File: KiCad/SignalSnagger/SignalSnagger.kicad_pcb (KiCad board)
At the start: 2 copper layers, 133.4 x 44.3 mm, 4 parts

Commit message: Rev 0.28
Adding footprints to schematic: ~10% done
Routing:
- added copper zone on In1.Cu, net (none)
- added copper zone on In2.Cu, net (none)
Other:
- copper layers 2 -> 4
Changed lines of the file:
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@@
 (kicad_pcb (version 20211014) (generator pcbnew)
   (general
-    (thickness 1.6)
+    (thickness 4.69)
   )
   (paper "A4")
   (layers
     (0 "F.Cu" signal)
+    (1 "In1.Cu" signal)
+    (2 "In2.Cu" signal)
     (31 "B.Cu" signal)
     (32 "B.Adhes" user "B.Adhesive")
@@
   )
   (setup
+    (stackup
+      (layer "F.SilkS" (type "Top Silk Screen"))
+      (layer "F.Paste" (type "Top Solder Paste"))
+      (layer "F.Mask" (type "Top Solder Mask") (thickness 0.01))
+      (layer "F.Cu" (type "copper") (thickness 0.035))
+      (layer "dielectric 1" (type "core") (thickness 1.51) (material "FR4") (epsilon_r 4.5) (loss_tangent 0.02))
+      (layer "In1.Cu" (type "copper") (thickness 0.035))
+      (layer "dielectric 2" (type "prepreg") (thickness 1.51) (material "FR4") (epsilon_r 4.5) (loss_tangent 0.02))
+      (layer "In2.Cu" (type "copper") (thickness 0.035))
+      (layer "dielectric 3" (type "core") (thickness 1.51) (material "FR4") (epsilon_r 4.5) (loss_tangent 0.02))
+      (layer "B.Cu" (type "copper") (thickness 0.035))
+      (layer "B.Mask" (type "Bottom Solder Mask") (thickness 0.01))
+      (layer "B.Paste" (type "Bottom Solder Paste"))
+      (layer "B.SilkS" (type "Bottom Silk Screen"))
+      (copper_finish "None")
+      (dielectric_constraints no)
+    )
     (pad_to_mask_clearance 0)
     (pcbplotparams
@@
     )
   )
+  (zone locked (net 0) (net_name "") (layers "In1.Cu" "In2.Cu") (hatch edge 0.508)
+    (connect_pads (clearance 0.508))
+    (min_thickness 0.254) (filled_areas_thickness no)
+    (fill yes (thermal_gap 0.508) (thermal_bridge_width 0.508))
+    (polygon
+      (pts
+        (xy 210.24 115.69)
+        (xy 208.01 117.92)
+        (xy 80.01 117.98)
+        (xy 77.69 115.66)
+        (xy 77.68 76.65)
+        (xy 79.99 74.38)
+        (xy 208 74.37)
+        (xy 210.25 76.61)
+      )
+    )
+  )
   (zone locked (net 0) (net_name "") (layer "B.Cu") (hatch edge 0.508)
     (connect_pads (clearance 0.508))
     (min_thickness 0.254) (filled_areas_thickness no)
-    (fill (thermal_gap 0.508) (thermal_bridge_width 0.508))
+    (fill yes (thermal_gap 0.508) (thermal_bridge_width 0.508))
     (polygon
       (pts

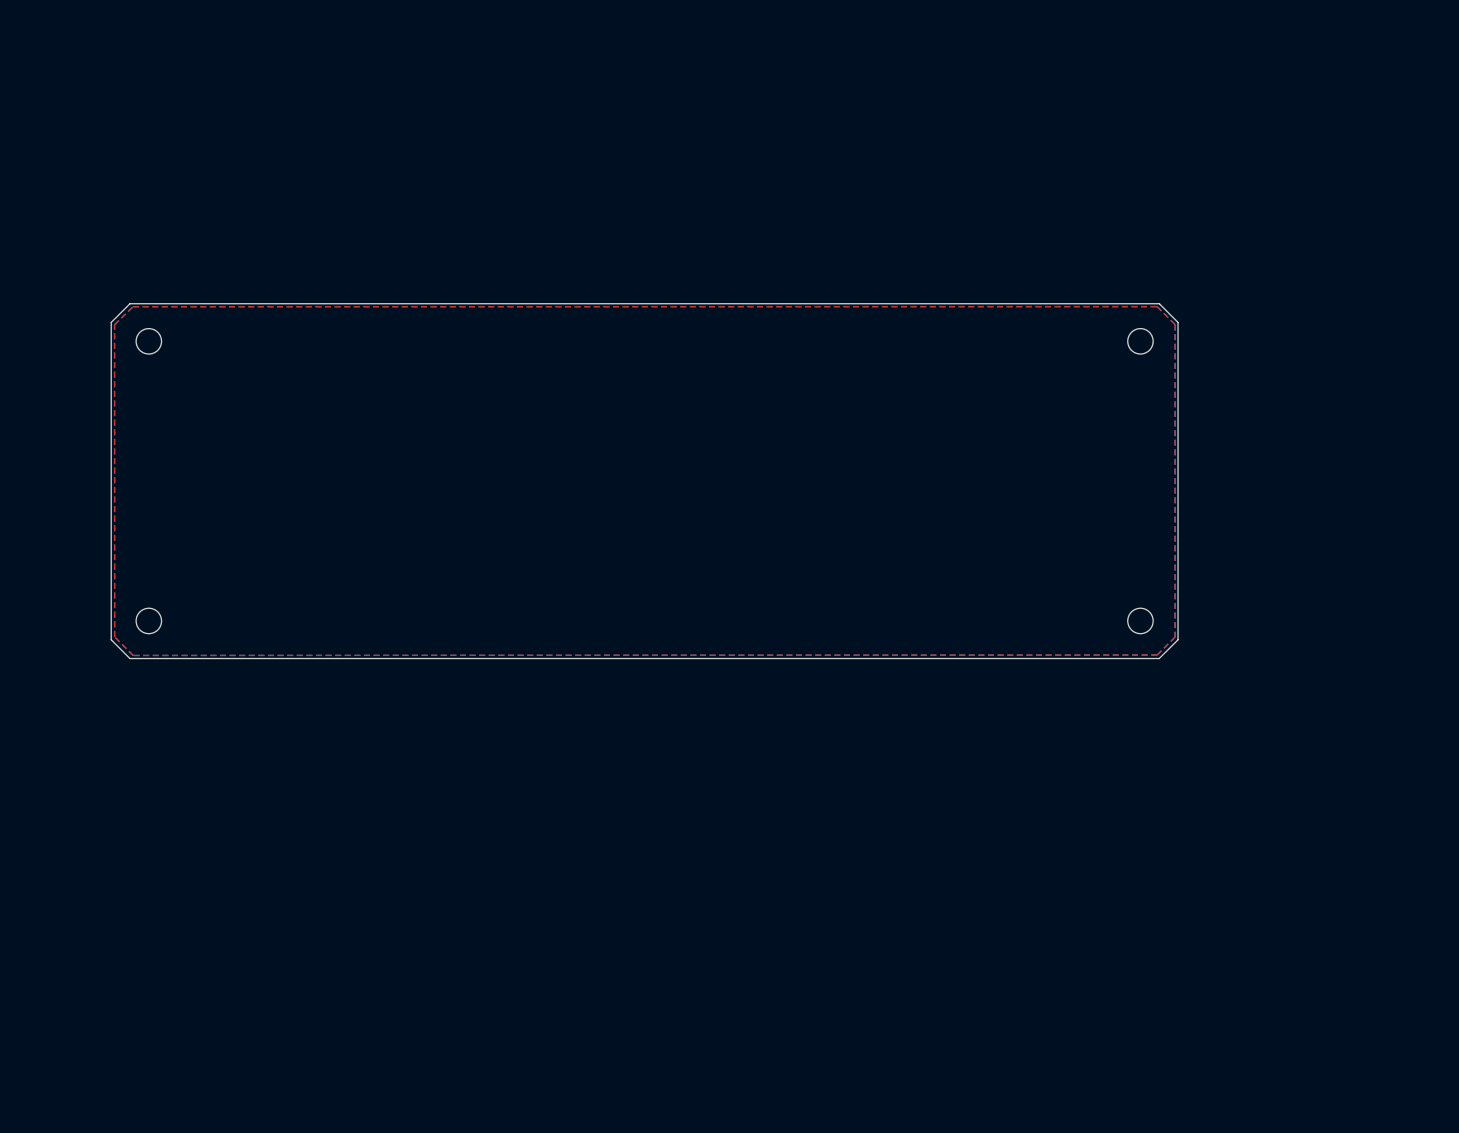
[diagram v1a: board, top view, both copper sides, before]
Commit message: Rev 0.301
PCB Updates - first import from schematic
Schematic Updates - fixes for various footprints
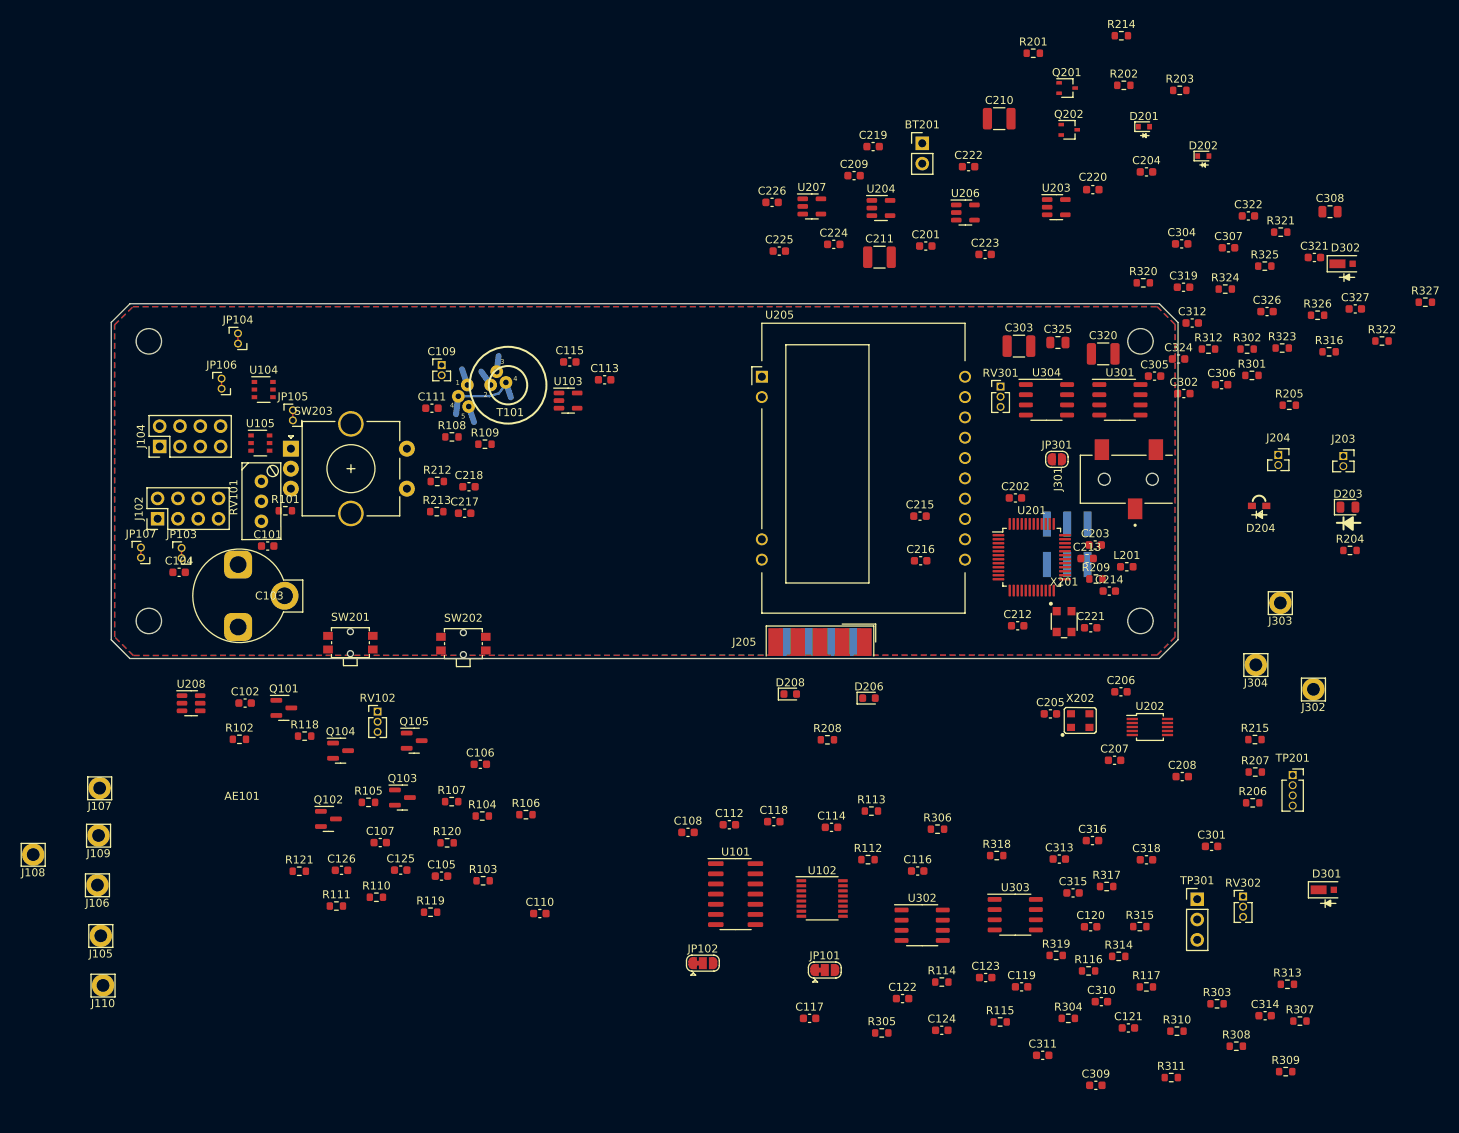
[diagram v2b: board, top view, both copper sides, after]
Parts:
- added AE101: Sense Ant., Oddities:Dummy_Empty, F.Cu at (93.5, 138.1)
- added BT201: Battery, Connector_PinHeader_2.54mm:PinHeader_1x02_P2.54mm_Vertical, F.Cu at (178.6, 54.0)
- added C101: 100pF, Capacitor_SMD:C_0603_1608Metric, F.Cu at (96.8, 104.3)
- added C102: 100nF, Capacitor_SMD:C_0603_1608Metric, F.Cu at (94.0, 123.9)
- added C103: 8.5-100pF, Capacitor_THT:VC07B, F.Cu at (93.1, 110.5)
- added C104: 51pF, Capacitor_SMD:C_0603_1608Metric, F.Cu at (85.8, 107.6)
- added C105: 10nF, Capacitor_SMD:C_0603_1608Metric, F.Cu at (118.5, 145.6)
- added C106: 10nF, Capacitor_SMD:C_0603_1608Metric, F.Cu at (123.4, 131.6)
- added C107: 10nF, Capacitor_SMD:C_0603_1608Metric, F.Cu at (110.9, 141.4)
- added C108: 100nF, Capacitor_SMD:C_0603_1608Metric, F.Cu at (149.4, 140.1)
- added C109: 2pF, Connector_PinHeader_1.27mm:PinHeader_1x02_P1.27mm_Vertical, F.Cu at (118.6, 81.7)
- added C110: 10nF, Capacitor_SMD:C_0603_1608Metric, F.Cu at (130.8, 150.2)
- added C111: 100nF, Capacitor_SMD:C_0603_1608Metric, F.Cu at (117.3, 87.1)
- added C112: 100nF, Capacitor_SMD:C_0603_1608Metric, F.Cu at (154.5, 139.1)
- added C113: 10uF, Capacitor_SMD:C_0603_1608Metric, F.Cu at (138.9, 83.5)
- added C114: 47nF, Capacitor_SMD:C_0603_1608Metric, F.Cu at (167.3, 139.5)
- added C115: 100nF, Capacitor_SMD:C_0603_1608Metric, F.Cu at (134.6, 81.3)
- added C116: 390pF, Capacitor_SMD:C_0603_1608Metric, F.Cu at (178.1, 144.9)
- added C117: 100nF, Capacitor_SMD:C_0603_1608Metric, F.Cu at (164.6, 163.3)
- added C118: 47nF, Capacitor_SMD:C_0603_1608Metric, F.Cu at (160.1, 138.8)
- added C119: 390pF, Capacitor_SMD:C_0603_1608Metric, F.Cu at (191.1, 159.4)
- added C120: 100nF, Capacitor_SMD:C_0603_1608Metric, F.Cu at (199.7, 151.9)
- added C121: 100nF, Capacitor_SMD:C_0603_1608Metric, F.Cu at (204.4, 164.5)
- added C122: 100nF, Capacitor_SMD:C_0603_1608Metric, F.Cu at (176.2, 160.9)
- added C123: 100nF, Capacitor_SMD:C_0603_1608Metric, F.Cu at (186.6, 158.2)
- added C124: 100nF, Capacitor_SMD:C_0603_1608Metric, F.Cu at (181.1, 164.8)
- added C125: 10uF, Capacitor_SMD:C_0603_1608Metric, F.Cu at (113.5, 144.8)
- added C126: 10uF, Capacitor_SMD:C_0603_1608Metric, F.Cu at (106.0, 144.8)
- added C201: 100nF, Capacitor_SMD:C_0603_1608Metric, F.Cu at (179.1, 66.8)
- added C202: 100nF, Capacitor_SMD:C_0603_1608Metric, F.Cu at (190.3, 98.3)
- added C203: 100nF, Capacitor_SMD:C_0603_1608Metric, F.Cu at (200.3, 104.2)
- added C204: 10nF, Capacitor_SMD:C_0603_1608Metric, F.Cu at (206.7, 57.5)
- added C205: 100nF, Capacitor_SMD:C_0603_1608Metric, F.Cu at (194.7, 125.3)
- added C206: 470nF, Capacitor_SMD:C_0603_1608Metric, F.Cu at (203.5, 122.5)
- added C207: 100nF, Capacitor_SMD:C_0603_1608Metric, F.Cu at (202.7, 131.1)
- added C208: 470nF, Capacitor_SMD:C_0603_1608Metric, F.Cu at (211.1, 133.1)
- added C209: 100nF, Capacitor_SMD:C_0603_1608Metric, F.Cu at (170.1, 58.0)
- added C210: 47uF, Capacitor_SMD:C_1210_3225Metric, F.Cu at (188.3, 50.9)
- added C211: 47uF, Capacitor_SMD:C_1210_3225Metric, F.Cu at (173.3, 68.2)
- added C212: 100nF, Capacitor_SMD:C_0603_1608Metric, F.Cu at (190.6, 114.3)
- added C213: 10uF, Capacitor_SMD:C_0603_1608Metric, F.Cu at (199.2, 105.9)
- added C214: 10nF, Capacitor_SMD:C_0603_1608Metric, F.Cu at (202.0, 109.9)
- added C215: 1uF, Capacitor_SMD:C_0603_1608Metric, F.Cu at (178.4, 100.6)
- added C216: 1uF, Capacitor_SMD:C_0603_1608Metric, F.Cu at (178.4, 106.1)
- added C217: 10nF, Capacitor_SMD:C_0603_1608Metric, F.Cu at (121.4, 100.2)
- added C218: 10nF, Capacitor_SMD:C_0603_1608Metric, F.Cu at (122.0, 96.9)
- added C219: 10nF, Capacitor_SMD:C_0603_1608Metric, F.Cu at (172.5, 54.4)
- added C220: 10nF, Capacitor_SMD:C_0603_1608Metric, F.Cu at (200.0, 59.8)
- added C221: 100nF, Capacitor_SMD:C_0603_1608Metric, F.Cu at (199.7, 114.5)
- added C222: 100nF, Capacitor_SMD:C_0603_1608Metric, F.Cu at (184.4, 56.9)
- added C223: 10nF, Capacitor_SMD:C_0603_1608Metric, F.Cu at (186.5, 67.8)
- added C224: 10uF, Capacitor_SMD:C_0603_1608Metric, F.Cu at (167.6, 66.6)
- added C225: 10uF, Capacitor_SMD:C_0603_1608Metric, F.Cu at (160.8, 67.4)
- added C226: 10uF, Capacitor_SMD:C_0603_1608Metric, F.Cu at (159.9, 61.3)
- added C301: 100nF, Capacitor_SMD:C_0603_1608Metric, F.Cu at (214.8, 141.8)
- added C302: 10nF, Capacitor_SMD:C_0603_1608Metric, F.Cu at (211.3, 85.2)
- added C303: 47uF, Capacitor_SMD:C_1210_3225Metric, F.Cu at (190.7, 79.3)
- added C304: 100nF, Capacitor_SMD:C_0603_1608Metric, F.Cu at (211.1, 66.5)
- added C305: 1uF, Capacitor_SMD:C_0603_1608Metric, F.Cu at (207.7, 83.1)
- added C306: 10uF, Capacitor_SMD:C_0603_1608Metric, F.Cu at (216.1, 84.1)
- added C307: 100nF, Capacitor_SMD:C_0603_1608Metric, F.Cu at (216.9, 67.0)
- added C308: 22uF, Capacitor_SMD:C_0805_2012Metric, F.Cu at (229.6, 62.5)
- added C309: 100nF, Capacitor_SMD:C_0603_1608Metric, F.Cu at (200.3, 171.7)
- added C310: 150nF, Capacitor_SMD:C_0603_1608Metric, F.Cu at (201.0, 161.2)
- added C311: 4.7nF, Capacitor_SMD:C_0603_1608Metric, F.Cu at (193.7, 168.0)
- added C312: 10uF, Capacitor_SMD:C_0603_1608Metric, F.Cu at (212.4, 76.4)
- added C313: 100nF, Capacitor_SMD:C_0603_1608Metric, F.Cu at (195.8, 143.4)
- added C314: 1uF, Capacitor_SMD:C_0603_1608Metric, F.Cu at (221.5, 163.0)
- added C315: 150nF, Capacitor_SMD:C_0603_1608Metric, F.Cu at (197.5, 147.7)
- added C316: 4.7nF, Capacitor_SMD:C_0603_1608Metric, F.Cu at (199.9, 141.1)
- added C318: 100nF, Capacitor_SMD:C_0603_1608Metric, F.Cu at (206.7, 143.5)
- added C319: 10nF, Capacitor_SMD:C_0603_1608Metric, F.Cu at (211.3, 72.0)
- added C320: 47uF, Capacitor_SMD:C_1210_3225Metric, F.Cu at (201.3, 80.3)
- added C321: 1uF, Capacitor_SMD:C_0603_1608Metric, F.Cu at (227.7, 68.2)
- added C322: 100nF, Capacitor_SMD:C_0603_1608Metric, F.Cu at (219.4, 63.0)
- added C324: 100nF, Capacitor_SMD:C_0603_1608Metric, F.Cu at (210.7, 80.9)
- added C325: 22uF, Capacitor_SMD:C_0805_2012Metric, F.Cu at (195.6, 78.9)
- added C326: 100nF, Capacitor_SMD:C_0603_1608Metric, F.Cu at (221.7, 75.0)
- added C327: 1uF, Capacitor_SMD:C_0603_1608Metric, F.Cu at (232.8, 74.7)
- added D201: 1N914WT, Diode_SMD:D_SOD-523, F.Cu at (206.4, 51.9)
- added D202: 1N914WT, Diode_SMD:D_SOD-523, F.Cu at (213.8, 55.5)
- added D203: Red LED, LED_SMD:LED_0805_2012Metric, F.Cu at (231.8, 99.4)
- added D204: Green LED, LED_SMD:LED_APDA1806SECK, F.Cu at (220.8, 99.3)
- added D206: ESD9B5.0ST5G_1, Diode_SMD:D_0603_1608Metric, F.Cu at (172.0, 123.3)
- added D208: ESD9B5.0ST5G_1, Diode_SMD:D_0603_1608Metric, F.Cu at (162.1, 122.8)
- added D301: MSS1P4-M3, Diode_SMD:DO-219AD, F.Cu at (229.2, 147.3)
- added D302: MSS1P4-M3, Diode_SMD:DO-219AD, F.Cu at (231.5, 69.0)
- added J102: Left, Connector_PinHeader_2.54mm:PinHeader_2x04_P2.54mm_Vertical, F.Cu at (83.1, 100.9)
- added J104: Right, Connector_PinHeader_2.54mm:PinHeader_2x04_P2.54mm_Vertical, F.Cu at (83.3, 91.9)
- added J105: 36-5005-ND, Connector_Pin:Pin_D1.6mm_L8.5mm_W2.8mm_FlatFork, F.Cu at (76.0, 153.0)
- added J106: 36-5006-ND, Connector_Pin:Pin_D1.6mm_L8.5mm_W2.8mm_FlatFork, F.Cu at (75.5, 146.7)
- added J107: 36-5006-ND, Connector_Pin:Pin_D1.6mm_L8.5mm_W2.8mm_FlatFork, F.Cu at (75.8, 134.6)
- added J108: 36-5005-ND, Connector_Pin:Pin_D1.6mm_L8.5mm_W2.8mm_FlatFork, F.Cu at (67.5, 142.9)
- added J109: 36-5006-ND, Connector_Pin:Pin_D1.6mm_L8.5mm_W2.8mm_FlatFork, F.Cu at (75.7, 140.5)
- added J110: 36-5006-ND, Connector_Pin:Pin_D1.6mm_L8.5mm_W2.8mm_FlatFork, F.Cu at (76.2, 159.2)
- added J203: Conn_01x02, Connector_PinSocket_1.27mm:PinSocket_1x02_P1.27mm_Vertical, F.Cu at (231.3, 93.0)
- added J204: Conn_01x02, Connector_PinSocket_1.27mm:PinSocket_1x02_P1.27mm_Vertical, F.Cu at (223.1, 92.9)
- added J205: DB9 Female, Connector_Dsub:DSUB-9_Female_EdgeMount_P2.77mm, F.Cu at (165.9, 116.3)
- added J301: 35RASMT2BHSNTRX, Connector_Audio:SWITCHCRAFT_35RASMT2BHSNTRX, F.Cu at (204.4, 96.0)
- added J302: 36-5005-ND, Connector_Pin:Pin_D1.6mm_L8.5mm_W2.8mm_FlatFork, F.Cu at (227.5, 122.2)
- added J303: 36-5005-ND, Connector_Pin:Pin_D1.6mm_L8.5mm_W2.8mm_FlatFork, F.Cu at (223.4, 111.4)
- added J304: 36-5006-ND, Connector_Pin:Pin_D1.6mm_L8.5mm_W2.8mm_FlatFork, F.Cu at (220.3, 119.2)
- added JP101: SolderJumper_3_Bridged12, Jumper:SolderJumper-3_P1.3mm_Bridged12_RoundedPad1.0x1.5mm, F.Cu at (166.5, 157.3)
- added JP102: SolderJumper_3_Bridged12, Jumper:SolderJumper-3_P1.3mm_Bridged12_RoundedPad1.0x1.5mm, F.Cu at (151.2, 156.4)
- added JP103: Jumper_2_Bridged, Jumper:Jumper_THT_1x02_P1.27mm_Vertical, F.Cu at (86.1, 104.5)
- added JP104: Jumper_2_Bridged, Jumper:Jumper_THT_1x02_P1.27mm_Vertical, F.Cu at (93.1, 77.7)
- added JP105: Jumper_2_Bridged, Jumper:Jumper_THT_1x02_P1.27mm_Vertical, F.Cu at (100.0, 87.3)
- added JP106: Jumper_2_Bridged, Jumper:Jumper_THT_1x02_P1.27mm_Vertical, F.Cu at (91.1, 83.4)
- added JP107: Jumper_2_Bridged, Jumper:Jumper_THT_1x02_P1.27mm_Vertical, F.Cu at (81.0, 104.5)
- added JP301: SolderJumper_2_Open, Jumper:SolderJumper-2_P1.3mm_Open_RoundedPad1.0x1.5mm, F.Cu at (195.5, 93.5)
- added L201: 10uH, Inductor_SMD:L_0603_1608Metric, F.Cu at (204.2, 106.9)
- added P201: ISP/PDI, Connector_PinHeader_2.54mm:PinHeader_2x03_P2.54mm_Vertical_SMD, B.Cu at (196.8, 104.1)
- added Q101: MMBT2222A, Package_TO_SOT_SMD:SOT-23, F.Cu at (98.8, 124.5)
- added Q102: MMBT2222A, Package_TO_SOT_SMD:SOT-23, F.Cu at (104.4, 138.4)
- added Q103: MMBT2222A, Package_TO_SOT_SMD:SOT-23, F.Cu at (113.7, 135.7)
- added Q104: MMBT2222A, Package_TO_SOT_SMD:SOT-23, F.Cu at (105.9, 129.9)
- added Q105: MMBT2222A, Package_TO_SOT_SMD:SOT-23, F.Cu at (115.1, 128.6)
- added Q201: BSS84W-7-F, Package_TO_SOT_SMD:SOT-323_SC-70, F.Cu at (196.8, 47.0)
- added Q202: BSS138W-7-F, Package_TO_SOT_SMD:SOT-323_SC-70, F.Cu at (197.0, 52.3)
- added R101: 100k, Resistor_SMD:R_0603_1608Metric, F.Cu at (99.0, 99.9)
- added R102: 1k, Resistor_SMD:R_0603_1608Metric, F.Cu at (93.3, 128.5)
- added R103: 10k, Resistor_SMD:R_0603_1608Metric, F.Cu at (123.8, 146.1)
- added R104: 22k, Resistor_SMD:R_0603_1608Metric, F.Cu at (123.6, 138.1)
- added R105: 10k, Resistor_SMD:R_0603_1608Metric, F.Cu at (109.4, 136.3)
- added R106: 100, Resistor_SMD:R_0603_1608Metric, F.Cu at (129.1, 137.9)
- added R107: 470, Resistor_SMD:R_0603_1608Metric, F.Cu at (119.8, 136.2)
- added R108: 10, Resistor_SMD:R_0603_1608Metric, F.Cu at (119.8, 90.7)
- added R109: 10, Resistor_SMD:R_0603_1608Metric, F.Cu at (124.0, 91.6)
- added R110: 4.7k, Resistor_SMD:R_0603_1608Metric, F.Cu at (110.4, 148.2)
- added R111: 4.7k, Resistor_SMD:R_0603_1608Metric, F.Cu at (105.4, 149.3)
- added R112: 49.9, Resistor_SMD:R_0603_1608Metric, F.Cu at (171.9, 143.5)
- added R113: 4.99k, Resistor_SMD:R_0603_1608Metric, F.Cu at (172.3, 137.4)
- added R114: 49.9, Resistor_SMD:R_0603_1608Metric, F.Cu at (181.1, 158.8)
- added R115: 4.99k, Resistor_SMD:R_0603_1608Metric, F.Cu at (188.4, 163.8)
- added R116: 100, Resistor_SMD:R_0603_1608Metric, F.Cu at (199.4, 157.4)
- added R117: 100, Resistor_SMD:R_0603_1608Metric, F.Cu at (206.7, 159.4)
- added R118: 49.9, Resistor_SMD:R_0603_1608Metric, F.Cu at (101.4, 128.1)
- added R119: 1k, Resistor_SMD:R_0603_1608Metric, F.Cu at (117.2, 150.1)
- added R120: 10k, Resistor_SMD:R_0603_1608Metric, F.Cu at (119.2, 141.4)
- added R121: 1k, Resistor_SMD:R_0603_1608Metric, F.Cu at (100.8, 144.9)
- added R201: 100k, Resistor_SMD:R_0603_1608Metric, F.Cu at (192.5, 42.7)
- added R202: 162k, Resistor_SMD:R_0603_1608Metric, F.Cu at (203.8, 46.7)
- added R203: 12.4k, Resistor_SMD:R_0603_1608Metric, F.Cu at (210.8, 47.3)
- added R204: 1k, Resistor_SMD:R_0603_1608Metric, F.Cu at (232.1, 104.8)
- added R205: 220, Resistor_SMD:R_0603_1608Metric, F.Cu at (224.5, 86.7)
- added R206: 10k, Resistor_SMD:R_0603_1608Metric, F.Cu at (219.9, 136.4)
- added R207: 10k, Resistor_SMD:R_0603_1608Metric, F.Cu at (220.3, 132.6)
- added R208: 47k, Resistor_SMD:R_0603_1608Metric, F.Cu at (166.8, 128.5)
- added R209: 100, Resistor_SMD:R_0603_1608Metric, F.Cu at (200.3, 108.4)
- added R212: 10k, Resistor_SMD:R_0603_1608Metric, F.Cu at (118.0, 96.2)
- added R213: 10k, Resistor_SMD:R_0603_1608Metric, F.Cu at (118.0, 100.0)
- added R214: 10k, Resistor_SMD:R_0603_1608Metric, F.Cu at (203.5, 40.5)
- added R215: 10k, Resistor_SMD:R_0603_1608Metric, F.Cu at (220.2, 128.5)
- added R301: 10k, Resistor_SMD:R_0603_1608Metric, F.Cu at (219.8, 83.0)
- added R302: 10, Resistor_SMD:R_0603_1608Metric, F.Cu at (219.2, 79.7)
- added R303: 10k, Resistor_SMD:R_0603_1608Metric, F.Cu at (215.5, 161.5)
- added R304: 4.7k, Resistor_SMD:R_0603_1608Metric, F.Cu at (196.9, 163.3)
- added R305: 7.5k, Resistor_SMD:R_0603_1608Metric, F.Cu at (173.6, 165.2)
- added R306: 51k, Resistor_SMD:R_0603_1608Metric, F.Cu at (180.6, 139.7)
- added R307: 330k, Resistor_SMD:R_0603_1608Metric, F.Cu at (225.8, 163.7)
- added R308: 10k, Resistor_SMD:R_0603_1608Metric, F.Cu at (217.9, 166.8)
- added R309: 51k, Resistor_SMD:R_0603_1608Metric, F.Cu at (224.1, 170.0)
- added R310: 49.9k, Resistor_SMD:R_0603_1608Metric, F.Cu at (210.5, 164.9)
- added R311: 10k, Resistor_SMD:R_0603_1608Metric, F.Cu at (209.8, 170.7)
- added R312: 10, Resistor_SMD:R_0603_1608Metric, F.Cu at (214.4, 79.7)
- added R313: 1k, Resistor_SMD:R_0603_1608Metric, F.Cu at (224.3, 159.1)
- added R314: 49.9k, Resistor_SMD:R_0603_1608Metric, F.Cu at (203.2, 155.6)
- added R315: 10k, Resistor_SMD:R_0603_1608Metric, F.Cu at (205.8, 151.9)
- added R316: 470, Resistor_SMD:R_0603_1608Metric, F.Cu at (229.5, 80.0)
- added R317: 4.7k, Resistor_SMD:R_0603_1608Metric, F.Cu at (201.7, 146.9)
- added R318: 7.5k, Resistor_SMD:R_0603_1608Metric, F.Cu at (187.9, 143.0)
- added R319: 51k, Resistor_SMD:R_0603_1608Metric, F.Cu at (195.4, 155.5)
- added R320: 10, Resistor_SMD:R_0603_1608Metric, F.Cu at (206.3, 71.4)
- added R321: 470, Resistor_SMD:R_0603_1608Metric, F.Cu at (223.4, 65.1)
- added R322: 10, Resistor_SMD:R_0603_1608Metric, F.Cu at (236.1, 78.7)
- added R323: 10, Resistor_SMD:R_0603_1608Metric, F.Cu at (223.6, 79.5)
- added R324: 330k, Resistor_SMD:R_0603_1608Metric, F.Cu at (216.5, 72.2)
- added R325: 10k, Resistor_SMD:R_0603_1608Metric, F.Cu at (221.5, 69.3)
- added R326: 1k, Resistor_SMD:R_0603_1608Metric, F.Cu at (228.1, 75.5)
- added R327: 51k, Resistor_SMD:R_0603_1608Metric, F.Cu at (241.5, 73.8)
- added RV101: 10k 10T, Potentiometer_THT:Bourns_PV36W_Multiturn_Pot, F.Cu at (96.0, 98.7)
- added RV102: np, Connector_PinHeader_1.27mm:PinHeader_1x03_P1.27mm_Vertical, F.Cu at (110.6, 125.0)
- added RV301: 100k, Connector_PinHeader_1.27mm:PinHeader_1x03_P1.27mm_Vertical, F.Cu at (188.4, 84.4)
- added RV302: 100k, Connector_PinHeader_1.27mm:PinHeader_1x03_P1.27mm_Vertical, F.Cu at (218.8, 148.1)
- added SW201: SW_SPST, Button_Switch_SMD:SW_SPST_TL1014BF160QG, F.Cu at (107.2, 116.4)
- added SW202: SW_SPST, Button_Switch_SMD:SW_SPST_TL1014BF160QG, F.Cu at (121.3, 116.5)
- added SW203: PEC12R-4225F-S0024, Rotary_Encoder:RotaryEncoder_Bourns_PEC12R-Switch_Vertical_CircularMountingHoles, F.Cu at (107.2, 94.6)
- added T101: Transformer_1P_SS, Oddities:FT-37_Core_3_windings_Horiz_TH, F.Cu at (126.9, 84.2)
- added TP201: I2C1, Connector_PinSocket_1.27mm:PinSocket_1x04_P1.27mm_Vertical, F.Cu at (224.9, 132.9)
- added TP301: Conn_01x03, Connector_PinHeader_2.54mm:PinHeader_1x03_P2.54mm_Vertical, F.Cu at (213.0, 148.4)
- added U101: 74HC74, Package_SO:SO-14_3.9x8.65mm_P1.27mm, F.Cu at (155.3, 147.8)
- added U102: QS3253QG8, Package_SO:SSOP-16_3.9x4.9mm_P0.635mm, F.Cu at (166.1, 148.4)
- added U103: REF4132B33, Package_TO_SOT_SMD:SOT-23-5, F.Cu at (134.4, 86.1)
- added U104: DG9422E, Package_SO:TSOP-6_1.65x3.05mm_P0.95mm, F.Cu at (96.3, 84.7)
- added U105: DG9422E, Package_SO:TSOP-6_1.65x3.05mm_P0.95mm, F.Cu at (95.9, 91.4)
- added U201: AVR128DA48, Package_QFP:TQFP-48_7x7mm_P0.5mm, F.Cu at (192.3, 105.7)
- added U202: SI5351, Package_SO:MSOP-10_3x3mm_P0.5mm, F.Cu at (207.1, 126.9)
- added U203: LP2985-5.0, Package_TO_SOT_SMD:SOT-23-5, F.Cu at (195.4, 61.9)
- added U204: LP2985-3.3, Package_TO_SOT_SMD:SOT-23-5, F.Cu at (173.5, 62.0)
- added U205: EA_DOGS104W-A, Display:EA_DOGS104X-A, F.Cu at (158.6, 83.1)
- added U206: LP2985-5.0, Package_TO_SOT_SMD:SOT-23-5, F.Cu at (184.0, 62.6)
- added U207: MAX1683EUK, Package_TO_SOT_SMD:SOT-23-5, F.Cu at (164.8, 61.9)
- added U208: TPS22810DBVT, Package_TO_SOT_SMD:SOT-23-6, F.Cu at (87.2, 124.0)
- added U301: LM386, Package_SO:SO-8_3.9x4.9mm_P1.27mm, F.Cu at (203.3, 86.0)
- added U302: TS912IDT, Package_SO:SO-8_3.9x4.9mm_P1.27mm, F.Cu at (178.6, 151.7)
- added U303: TS912IDT, Package_SO:SO-8_3.9x4.9mm_P1.27mm, F.Cu at (190.3, 150.4)
- added U304: LM386, Package_SO:SO-8_3.9x4.9mm_P1.27mm, F.Cu at (194.2, 86.0)
- added X201: ECS-327TXO-30-TR, Oscillator:Oscillator_SMD_ECS_327TXO, F.Cu at (196.4, 113.7)
- added X202: 25 MHz, Crystal:Crystal_SMD_TXETCLSANF-4Pin, F.Cu at (198.4, 126.1)
